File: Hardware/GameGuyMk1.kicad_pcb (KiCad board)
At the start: 2 copper layers, 29 parts, among them J1 AVR-ISP-6, SW1 POWER, SW2 Left, SW3 Right, SW4 Up, SW5 Down, SW6 Btn_A, SW7 Btn_B, SW8 Play, SW9 Esc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

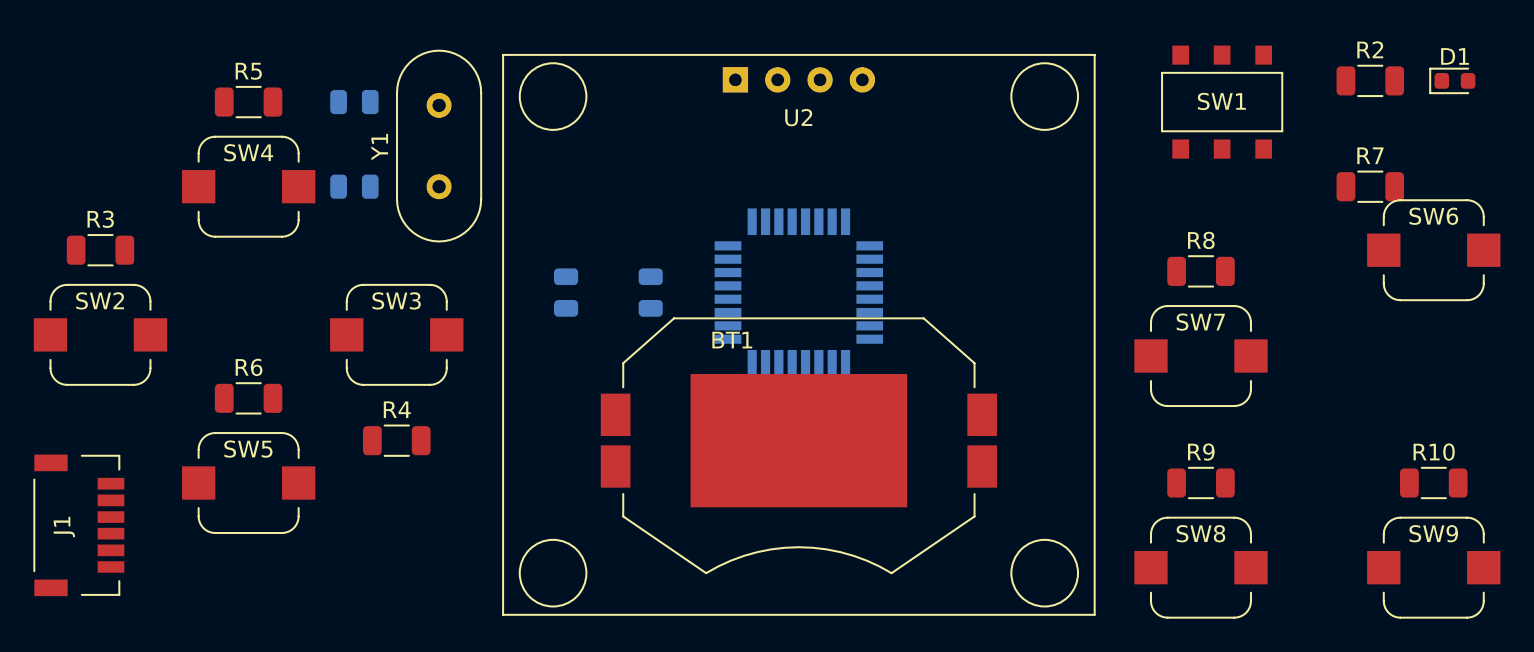
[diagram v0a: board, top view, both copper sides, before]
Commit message: Footprints updated for hand soldering
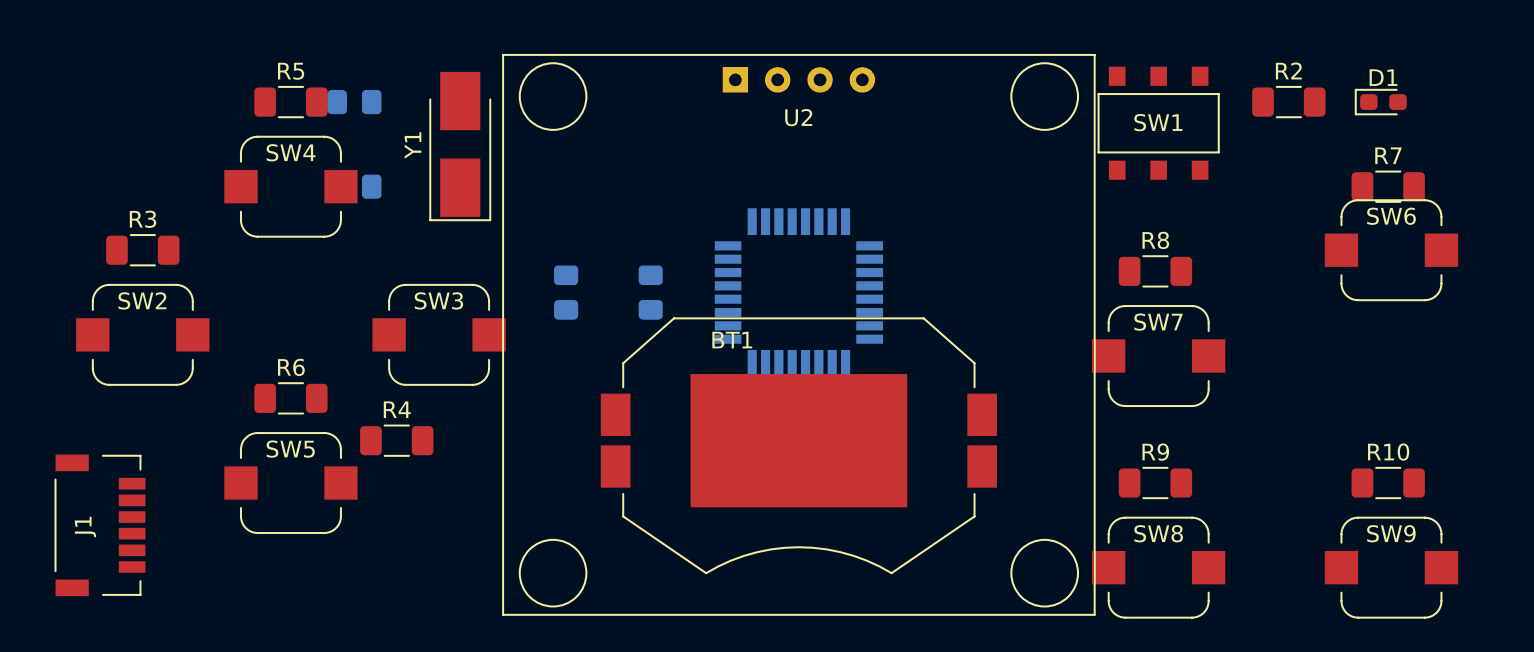
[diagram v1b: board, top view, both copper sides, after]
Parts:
- C1, C2, C3, C4: footprint Capacitor_SMD:C_0805_2012Metric -> Capacitor_SMD:C_0805_2012Metric_Pad1.18x1.45mm_HandSolder
- D1: footprint LED_SMD:LED_0603_1608Metric -> LED_SMD:LED_0603_1608Metric_Pad1.05x0.95mm_HandSolder
- R1, R10, R2, R3, R4, R5, R6, R7, R8, R9: footprint Resistor_SMD:R_1206_3216Metric -> Resistor_SMD:R_1206_3216Metric_Pad1.30x1.75mm_HandSolder
- Y1: footprint Crystal:Crystal_HC49-4H_Vertical -> Crystal:Crystal_SMD_5032-2Pin_5.0x3.2mm_HandSoldering
- moved R2 5.05 mm to (250.4, 104.1)
- moved D1 4.48 mm to (256.1, 104.1)
- moved SW1 4.02 mm to (242.6, 105.4)
- moved Y1 2.84 mm to (200.7, 106.7)
- moved R8 2.73 mm to (242.4, 114.3)
- moved R9 2.73 mm to (242.4, 127.0)
- moved R10 2.73 mm to (256.3, 127.0)
- moved R3 2.54 mm to (181.6, 113.0)
- moved SW2 2.54 mm to (181.6, 118.1)
- moved SW7 2.54 mm to (242.6, 119.4)
- moved SW8 2.54 mm to (242.6, 132.1)
- moved R5 2.54 mm to (190.5, 104.1)
- moved R6 2.54 mm to (190.5, 121.9)
- moved SW3 2.54 mm to (199.4, 118.1)
- moved SW4 2.54 mm to (190.5, 109.2)
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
